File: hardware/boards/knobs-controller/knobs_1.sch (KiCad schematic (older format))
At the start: 50 parts, among them J1 ZX62-AB-5PA(31), J10 Conn_01x01_Female, J11 Conn_01x01_Female, J12 Conn_01x01_Female, J13 Conn_01x01_Female, J14 Conn_01x01_Female, J15 Conn_01x01_Female, J16 Conn_01x01_Female, J17 Conn_01x01_Female, J18 Conn_01x01_Female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

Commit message: 1.8 work-in-progress
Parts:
- C1, C2, C4, C5: footprint footprints:RESISTOR-NICK_C0805 -> Capacitor_SMD:C_0805_2012Metric
- C3: footprint footprints:C0805 -> Capacitor_SMD:C_0805_2012Metric
- C6: footprint footprints:RESISTOR-NICK_C1206 -> Capacitor_SMD:C_1206_3216Metric
- R1, R7: footprint footprints:RESISTOR-NICK_R0805 -> Resistor_SMD:R_0805_2012Metric
- R2, R3, R4, R5, R6: footprint footprints:R0805 -> Resistor_SMD:R_0805_2012Metric
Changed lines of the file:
@@
 F 0 "C4" V 3211 5699 59  0000 L TNN
 F 1 "20pF" V 3210 5500 59  0000 R TNN
-F 2 "footprints:RESISTOR-NICK_C0805" H 3200 5600 50  0001 C CNN
+F 2 "Capacitor_SMD:C_0805_2012Metric" H 3200 5600 50  0001 C CNN
 F 3 "" H 3200 5600 50  0001 C CNN
 	1    3200 5600
@@
 F 0 "C2" H 3220 2515 59  0000 L BNN
 F 1 "1nF" H 3220 2485 59  0000 L TNN
-F 2 "footprints:RESISTOR-NICK_C0805" H 3100 2500 50  0001 C CNN
+F 2 "Capacitor_SMD:C_0805_2012Metric" H 3100 2500 50  0001 C CNN
 F 3 "" H 3100 2500 50  0001 C CNN
 	1    3100 2500
@@
 F 0 "C6" H 3820 2515 59  0000 L BNN
 F 1 "1nF" H 3820 2485 59  0000 L TNN
-F 2 "footprints:RESISTOR-NICK_C1206" H 3700 2500 50  0001 C CNN
+F 2 "Capacitor_SMD:C_1206_3216Metric" H 3700 2500 50  0001 C CNN
 F 3 "" H 3700 2500 50  0001 C CNN
 	1    3700 2500
@@
 F 0 "C5" V 3180 6100 59  0000 L BNN
 F 1 "20pF" V 3180 5900 59  0000 R BNN
-F 2 "footprints:RESISTOR-NICK_C0805" H 3200 6000 50  0001 C CNN
+F 2 "Capacitor_SMD:C_0805_2012Metric" H 3200 6000 50  0001 C CNN
 F 3 "" H 3200 6000 50  0001 C CNN
 	1    3200 6000
@@
 F 0 "C1" V 1400 4603 59  0000 L CNN
 F 1 "4.7nF" V 1500 4597 59  0000 L CNN
-F 2 "footprints:RESISTOR-NICK_C0805" H 1400 4500 50  0001 C CNN
+F 2 "Capacitor_SMD:C_0805_2012Metric" H 1400 4500 50  0001 C CNN
 F 3 "" H 1400 4500 50  0001 C CNN
 F 4 "1KV" V 1605 4597 59  0001 L CNN "VOLTAGE"
@@
 F 0 "R1" V 1840 4430 59  0000 R CNN
 F 1 "1M" V 1740 4430 59  0000 R CNN
-F 2 "footprints:RESISTOR-NICK_R0805" H 1800 4500 50  0001 C CNN
+F 2 "Resistor_SMD:R_0805_2012Metric" H 1800 4500 50  0001 C CNN
 F 3 "" H 1800 4500 50  0001 C CNN
 	1    1800 4500
@@
 F 0 "R7" H 7450 4850 59  0000 C BNN
 F 1 "330R" H 7450 4750 59  0000 C TNN
-F 2 "footprints:RESISTOR-NICK_R0805" H 7450 4800 50  0001 C CNN
+F 2 "Resistor_SMD:R_0805_2012Metric" H 7450 4800 50  0001 C CNN
 F 3 "" H 7450 4800 50  0001 C CNN
 	1    7450 4800
@@
 F 0 "R2" H 2900 8650 59  0000 C BNN
 F 1 "39R" H 2900 8550 59  0000 C TNN
-F 2 "footprints:R0805" H 2900 8600 50  0001 C CNN
+F 2 "Resistor_SMD:R_0805_2012Metric" H 2900 8600 50  0001 C CNN
 F 3 "" H 2900 8600 50  0001 C CNN
 	1    2900 8600
@@
 F 0 "R3" H 2900 9150 59  0000 C BNN
 F 1 "330R" H 2900 9050 59  0000 C TNN
-F 2 "footprints:R0805" H 2900 9100 50  0001 C CNN
+F 2 "Resistor_SMD:R_0805_2012Metric" H 2900 9100 50  0001 C CNN
 F 3 "" H 2900 9100 50  0001 C CNN
 	1    2900 9100
@@
 F 0 "C3" H 3220 9515 59  0000 L BNN
 F 1 "100nF" H 3220 9485 59  0000 L TNN
-F 2 "footprints:C0805" H 3100 9500 50  0001 C CNN
+F 2 "Capacitor_SMD:C_0805_2012Metric" H 3100 9500 50  0001 C CNN
 F 3 "" H 3100 9500 50  0001 C CNN
 	1    3100 9500
@@
 F 0 "R6" H 3300 9150 59  0000 C BNN
 F 1 "330R" H 3300 9050 59  0000 C TNN
-F 2 "footprints:R0805" H 3300 9100 50  0001 C CNN
+F 2 "Resistor_SMD:R_0805_2012Metric" H 3300 9100 50  0001 C CNN
 F 3 "" H 3300 9100 50  0001 C CNN
 	1    3300 9100
@@
 F 0 "R4" H 2890 7810 59  0000 R BNN
 F 1 "1K" H 3110 7810 59  0000 L BNN
-F 2 "footprints:R0805" H 3000 7800 50  0001 C CNN
+F 2 "Resistor_SMD:R_0805_2012Metric" H 3000 7800 50  0001 C CNN
 F 3 "" H 3000 7800 50  0001 C CNN
 	1    3000 7800
@@
 F 0 "R5" H 2990 7810 59  0000 R BNN
 F 1 "10K" H 3210 7810 59  0000 L BNN
-F 2 "footprints:R0805" H 3100 7800 50  0001 C CNN
+F 2 "Resistor_SMD:R_0805_2012Metric" H 3100 7800 50  0001 C CNN
 F 3 "" H 3100 7800 50  0001 C CNN
 	1    3100 7800

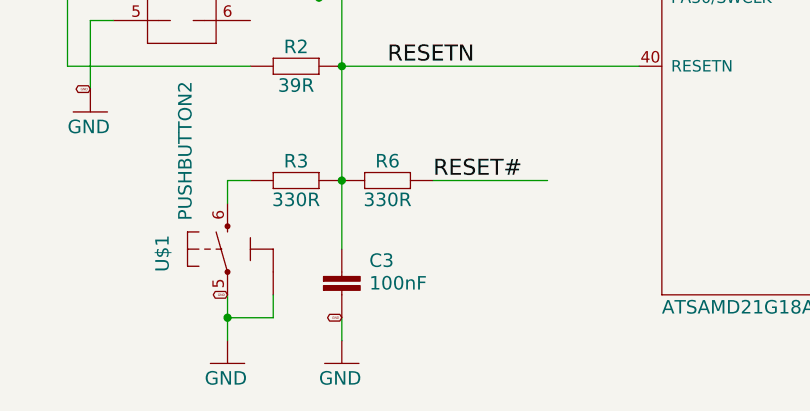
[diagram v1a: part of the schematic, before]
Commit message: 100nF changed to 0.1uF
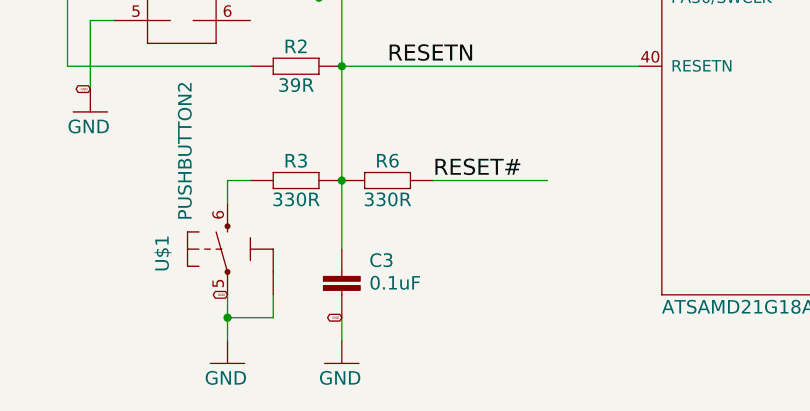
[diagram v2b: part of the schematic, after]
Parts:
- C3: value 100nF -> 0.1uF
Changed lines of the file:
@@
 AR Path="/5D86641C/B3C17CCA" Ref="C3"  Part="1"
 F 0 "C3" H 3220 9515 59  0000 L BNN
-F 1 "100nF" H 3220 9485 59  0000 L TNN
+F 1 "0.1uF" H 3220 9485 59  0000 L TNN
 F 2 "Capacitor_SMD:C_0805_2012Metric" H 3100 9500 50  0001 C CNN
 F 3 "" H 3100 9500 50  0001 C CNN

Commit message: changed c6 to 0805, updates to footprints to simplify BOM
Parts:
- C6: footprint Capacitor_SMD:C_1206_3216Metric -> Capacitor_SMD:C_0805_2012Metric; symbol knobs-eagle-import:RESISTOR-NICK_C-EUC1206 -> knobs-eagle-import:RESISTOR-NICK_C-EUC0805
- R4: value 1K -> 1k
- R5: value 10K -> 10k
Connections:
- net labels removed: VUSB
- no-connect marks 0 -> 4
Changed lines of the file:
@@
 	3700 2300 4100 2300
 Connection ~ 3700 2300
-Text GLabel 3600 2300 0    10   BiDi ~ 0
-VUSB
 Wire Wire Line
 	3600 5700 3600 5600
@@
 $EndComp
 $Comp
-L knobs-eagle-import:RESISTOR-NICK_C-EUC1206 C?
+L knobs-eagle-import:RESISTOR-NICK_C-EUC0805 C?
 U 1 1 7A89AA92
 P 3700 2500
@@
 F 0 "C6" H 3820 2515 59  0000 L BNN
 F 1 "1nF" H 3820 2485 59  0000 L TNN
-F 2 "Capacitor_SMD:C_1206_3216Metric" H 3700 2500 50  0001 C CNN
+F 2 "Capacitor_SMD:C_0805_2012Metric" H 3700 2500 50  0001 C CNN
 F 3 "" H 3700 2500 50  0001 C CNN
 	1    3700 2500
@@
 AR Path="/5D86641C/23ED3AB9" Ref="R4"  Part="1"
 F 0 "R4" H 2890 7810 59  0000 R BNN
-F 1 "1K" H 3110 7810 59  0000 L BNN
+F 1 "1k" H 3110 7810 59  0000 L BNN
 F 2 "Resistor_SMD:R_0805_2012Metric" H 3000 7800 50  0001 C CNN
 F 3 "" H 3000 7800 50  0001 C CNN
@@
 AR Path="/5D86641C/767DCB21" Ref="R5"  Part="1"
 F 0 "R5" H 2990 7810 59  0000 R BNN
-F 1 "10K" H 3210 7810 59  0000 L BNN
+F 1 "10k" H 3210 7810 59  0000 L BNN
 F 2 "Resistor_SMD:R_0805_2012Metric" H 3100 7800 50  0001 C CNN
 F 3 "" H 3100 7800 50  0001 C CNN
@@
 Connection ~ 14700 9400
 Connection ~ 14700 9300
+NoConn ~ 6400 5000
+NoConn ~ 4400 3400
+NoConn ~ 2700 8400
+NoConn ~ 1600 3400
 Wire Bus Line
 	13800 8200 13800 9600
